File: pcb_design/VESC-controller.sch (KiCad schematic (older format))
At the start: 26 parts, among them J1 GATE_DRIVER_CONN_U, J2 GATE_DRIVER_CONN_V, J3 GATE_DRIVER_CONN_W, J4 micro USB, J5 ACCEL, J6 REGEN, J7 12V, J8 V_BUS, P1 HALL/Encoder, P101 CANBUS, P2 Resolver, P3 PWR_COMM

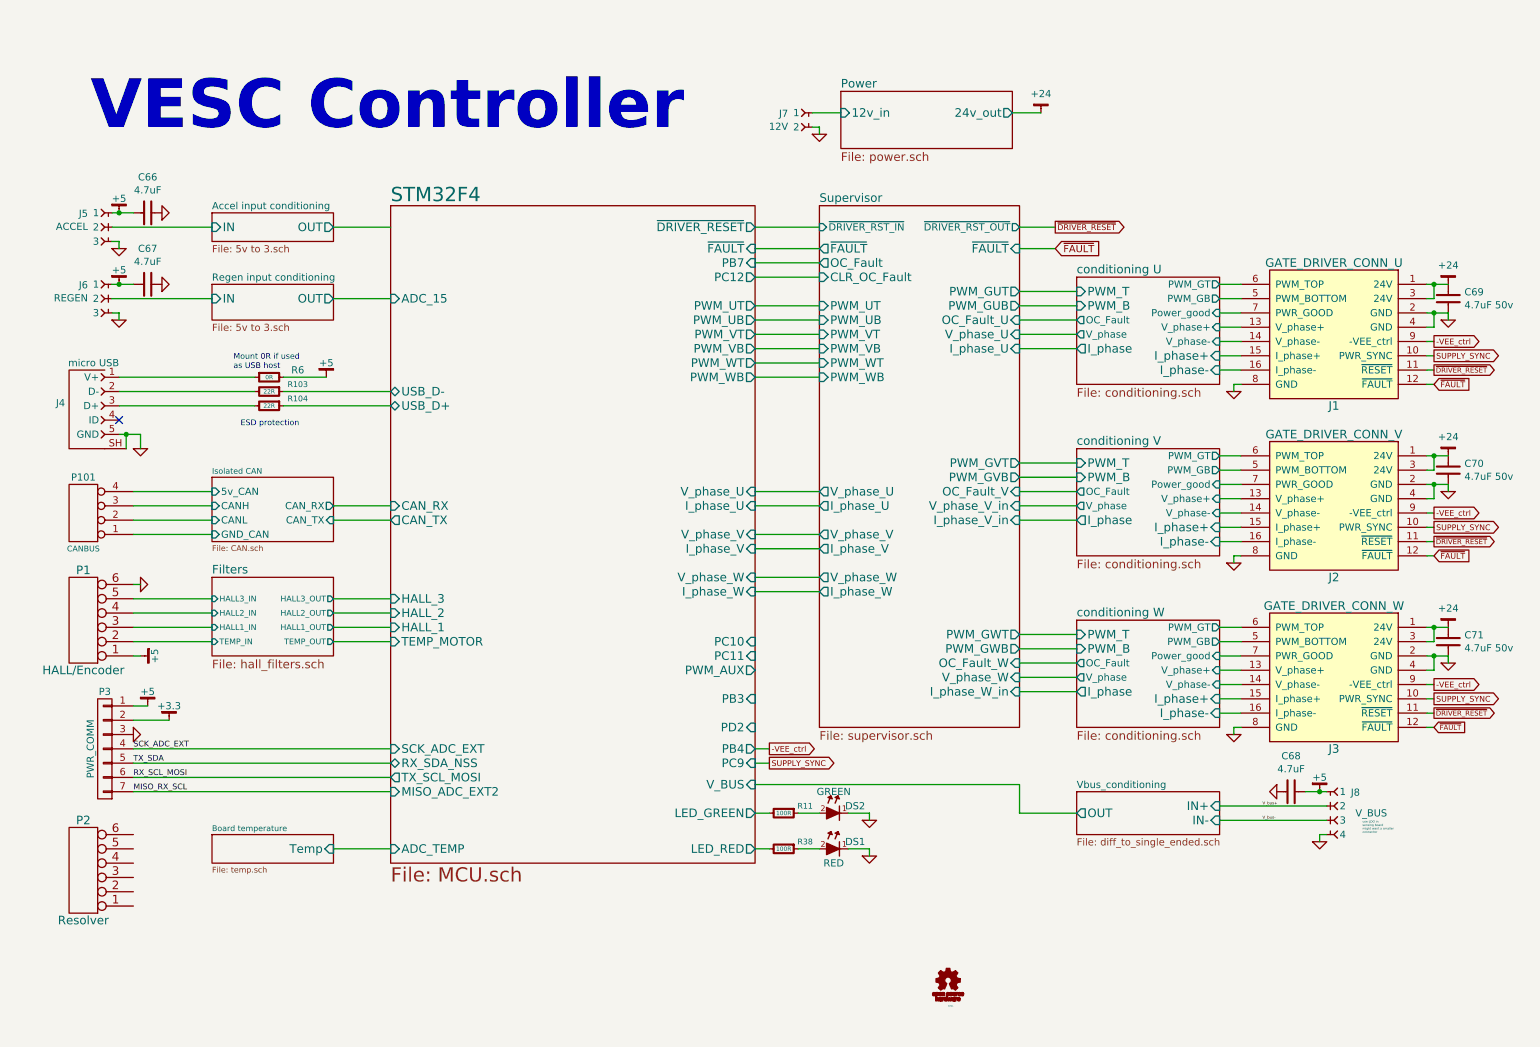
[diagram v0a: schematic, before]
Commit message: More layout. Changed LED pin. Added placeholder for a resolver IC
Signed-off-by: Marcos Chaparro <mchaparro@paltatech.com>
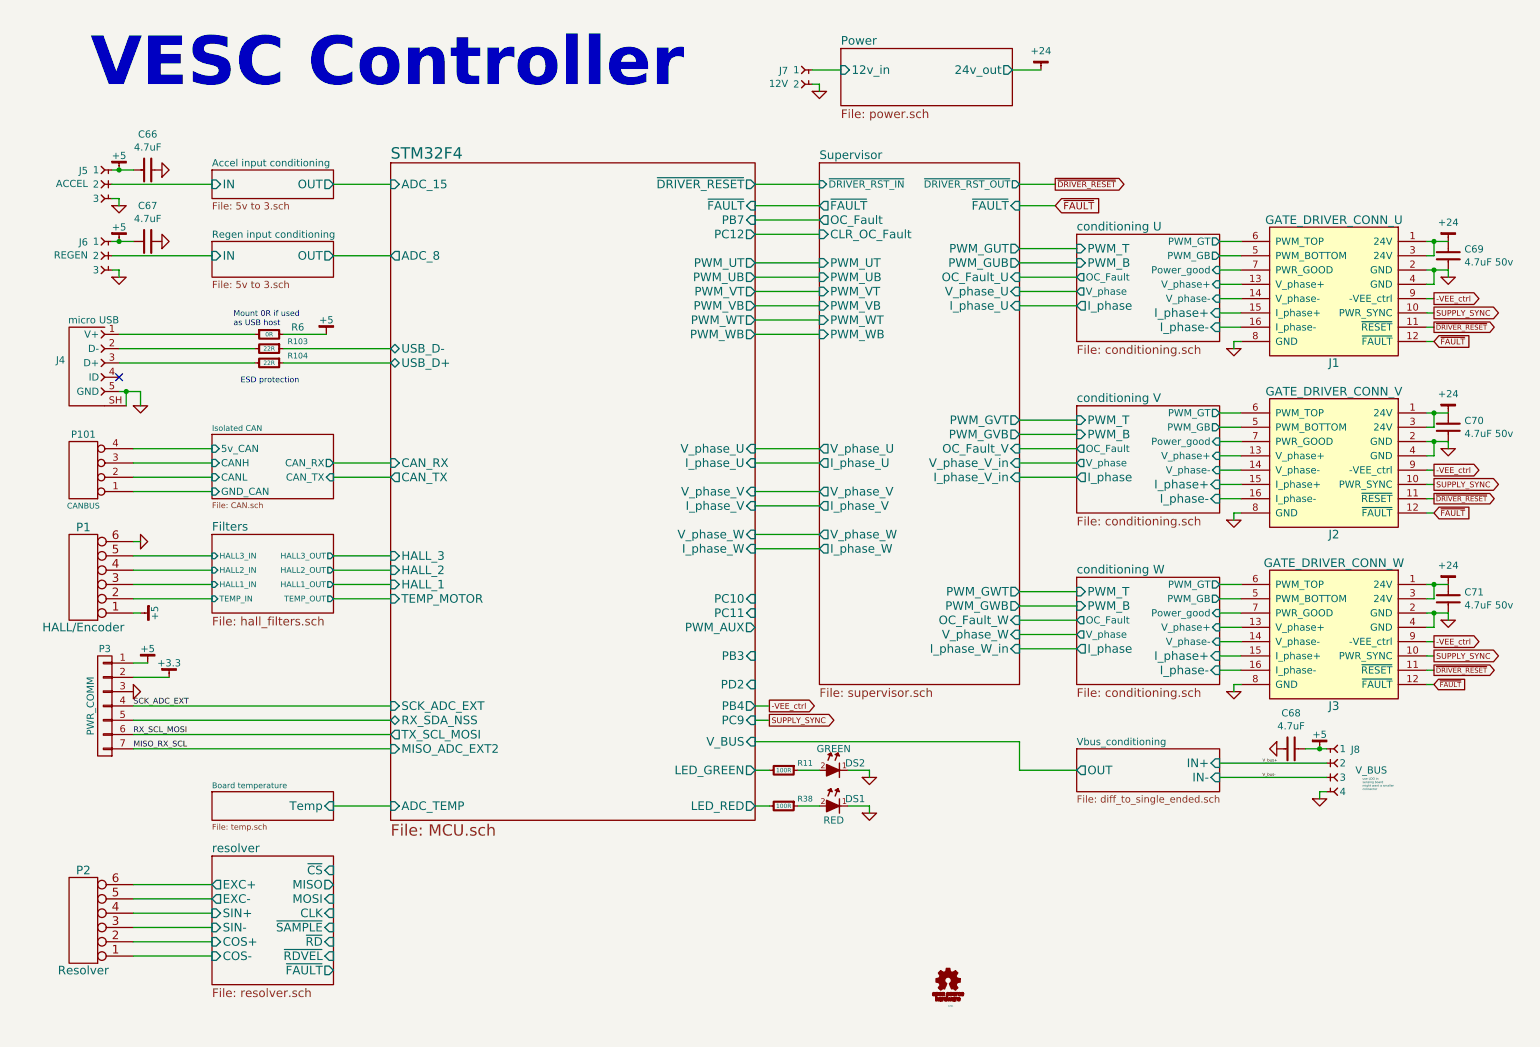
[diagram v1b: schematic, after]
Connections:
- net resolver/COS-: now reaches P2.1
- net resolver/COS+: now reaches P2.2
- net resolver/SIN-: now reaches P2.3
- net resolver/SIN+: now reaches P2.4
- net resolver/EXC-: now reaches P2.5
- net resolver/EXC+: now reaches P2.6
- net TX_SDA renamed STM32F4/RX_SDA_NSS
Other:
- moved on the sheet: C66, C67, C68, C69, C70, C71, DS1, DS2, J1, J2, J3, J4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

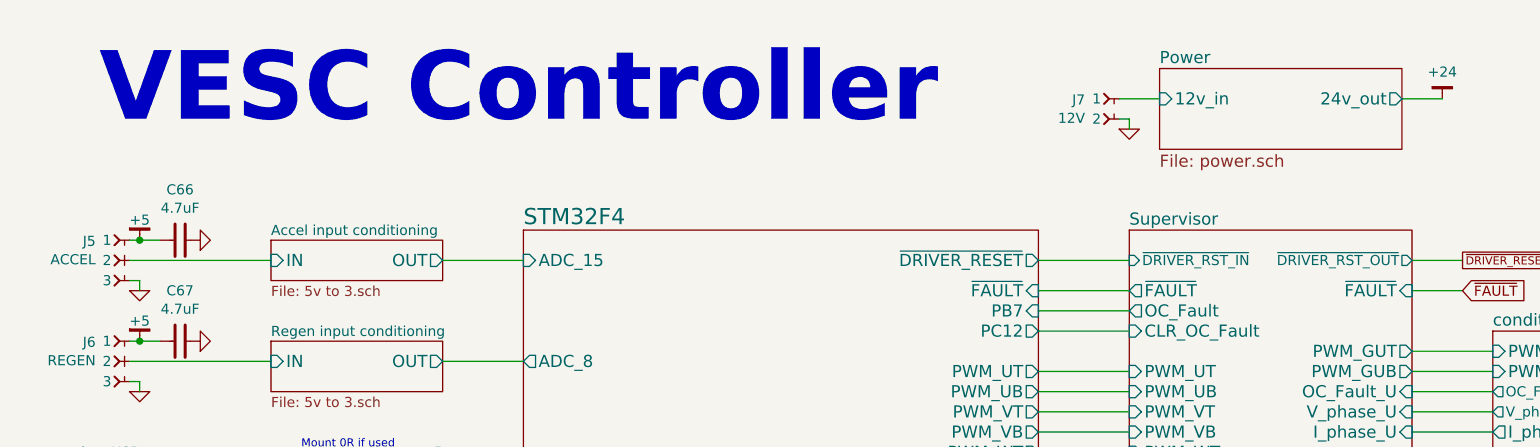
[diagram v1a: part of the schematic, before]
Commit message: Added reverse polarity protection on the isolated side of CON connector. Also, more layout
Signed-off-by: Marcos Chaparro <mchaparro@paltatech.com>
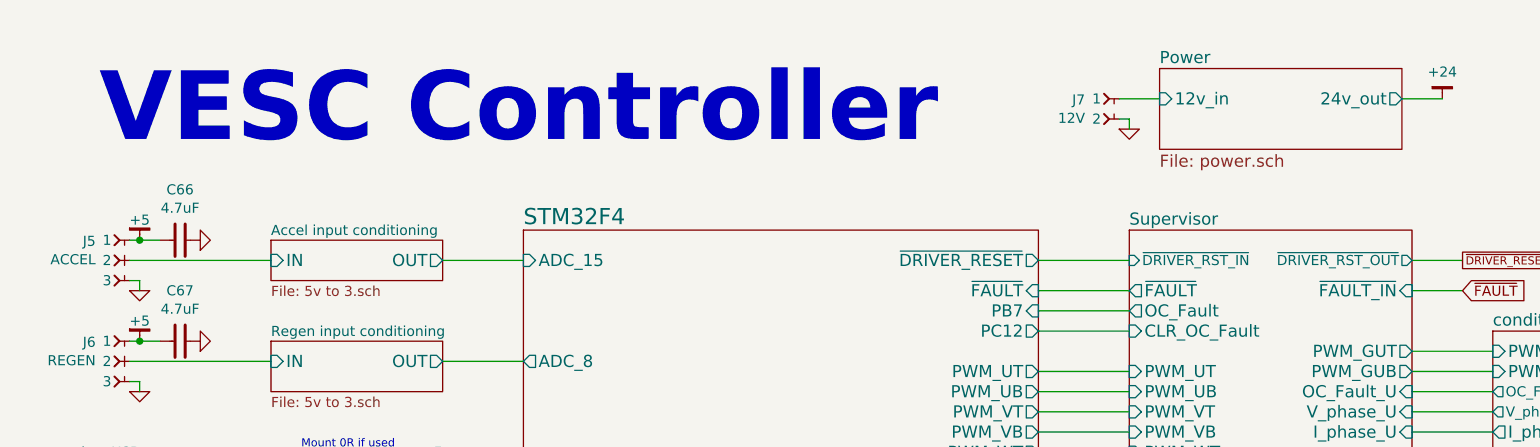
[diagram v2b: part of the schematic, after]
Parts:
- SYM1: footprint mech:OSHW-10mm -> (none)
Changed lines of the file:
@@
 $EndComp
 $Comp
-L GND-RESCUE-BLDC_4 #PWR01
+L GND-RESCUE-BLDC_4 #PWR7
 U 1 1 522DA053
 P 1500 4100
-F 0 "#PWR01" H 1500 4100 30  0001 C CNN
+F 0 "#PWR7" H 1500 4100 30  0001 C CNN
 F 1 "GND" H 1500 4030 30  0001 C CNN
 F 2 "" H 1500 4100 60  0001 C CNN
@@
 $EndComp
 $Comp
-L GND-RESCUE-BLDC_4 #PWR02
+L GND-RESCUE-BLDC_4 #PWR5
 U 1 1 522DA0E2
 P 1450 5150
-F 0 "#PWR02" H 1450 5150 30  0001 C CNN
+F 0 "#PWR5" H 1450 5150 30  0001 C CNN
 F 1 "GND" H 1450 5080 30  0001 C CNN
 F 2 "" H 1450 5150 60  0001 C CNN
@@
 $EndComp
 $Comp
-L GND-RESCUE-BLDC_4 #PWR03
+L GND-RESCUE-BLDC_4 #PWR6
 U 1 1 522DA0FC
 P 1500 3150
-F 0 "#PWR03" H 1500 3150 30  0001 C CNN
+F 0 "#PWR6" H 1500 3150 30  0001 C CNN
 F 1 "GND" H 1500 3080 30  0001 C CNN
 F 2 "" H 1500 3150 60  0001 C CNN
@@
 $EndComp
 $Comp
-L GND-RESCUE-BLDC_4 #PWR04
+L GND-RESCUE-BLDC_4 #PWR16
 U 1 1 53FC131A
 P 6600 6000
-F 0 "#PWR04" H 6600 6000 30  0001 C CNN
+F 0 "#PWR16" H 6600 6000 30  0001 C CNN
 F 1 "GND" H 6600 5930 30  0001 C CNN
 F 2 "" H 6600 6000 60  0001 C CNN
@@
 MISO_RX_SCL
 $Comp
-L GND #PWR05
+L GND #PWR25
 U 1 1 58876637
 P 10650 2250
-F 0 "#PWR05" H 10650 2250 30  0001 C CNN
+F 0 "#PWR25" H 10650 2250 30  0001 C CNN
 F 1 "GND" H 10650 2180 30  0001 C CNN
 F 2 "" H 10650 2250 60  0000 C CNN
@@
 F13 "I_phase-" I R 9050 2600 60
 $EndSheet
-Text Notes 1150 950  0    340  ~ 68
+Text Notes 1150 1050 0    340  ~ 68
 VESC Controller
 Wire Wire Line
@@
 F16 "OC_Fault_W" I R 7650 4650 60
 F17 "OC_Fault" O L 6250 1850 60
-F18 "~FAULT" I R 7650 1750 60
-F19 "~FAULT" O L 6250 1750 60
-F20 "V_phase_U" I R 7650 2350 60
-F21 "V_phase_U" O L 6250 3450 60
-F22 "V_phase_V" O L 6250 3750 60
-F23 "V_phase_W" O L 6250 4050 60
-F24 "V_phase_W" I R 7650 4750 60
-F25 "I_phase_U" I R 7650 2450 60
-F26 "I_phase_U" O L 6250 3550 60
-F27 "I_phase_V_in" I R 7650 3650 60
-F28 "I_phase_W_in" I R 7650 4850 60
-F29 "I_phase_V" O L 6250 3850 60
-F30 "I_phase_W" O L 6250 4150 60
-F31 "V_phase_V_in" I R 7650 3550 60
-F32 "CLR_OC_Fault" I L 6250 1950 60
-F33 "~DRIVER_RST_OUT" O R 7650 1600 50
-F34 "~DRIVER_RST_IN" I L 6250 1600 50
+F18 "~FAULT" O L 6250 1750 60
+F19 "V_phase_U" I R 7650 2350 60
+F20 "V_phase_U" O L 6250 3450 60
+F21 "V_phase_V" O L 6250 3750 60
+F22 "V_phase_W" O L 6250 4050 60
+F23 "V_phase_W" I R 7650 4750 60
+F24 "I_phase_U" I R 7650 2450 60
+F25 "I_phase_U" O L 6250 3550 60
+F26 "I_phase_V_in" I R 7650 3650 60
+F27 "I_phase_W_in" I R 7650 4850 60
+F28 "I_phase_V" O L 6250 3850 60
+F29 "I_phase_W" O L 6250 4150 60
+F30 "V_phase_V_in" I R 7650 3550 60
+F31 "CLR_OC_Fault" I L 6250 1950 60
+F32 "~DRIVER_RST_OUT" O R 7650 1600 50
+F33 "~DRIVER_RST_IN" I L 6250 1600 50
+F34 "~FAULT_IN" I R 7650 1750 60
 $EndSheet
 Wire Wire Line
@@
 	9200 2400 9050 2400
 $Comp
-L GND #PWR06
+L GND #PWR18
 U 1 1 588B9E09
 P 9150 2750
-F 0 "#PWR06" H 9150 2750 30  0001 C CNN
+F 0 "#PWR18" H 9150 2750 30  0001 C CNN
 F 1 "GND" H 9150 2680 30  0001 C CNN
 F 2 "" H 9150 2750 60  0000 C CNN
@@
 	9200 2600 9050 2600
 $Comp
-L GND #PWR07
+L GND #PWR27
 U 1 1 588C277E
 P 10650 3450
-F 0 "#PWR07" H 10650 3450 30  0001 C CNN
+F 0 "#PWR27" H 10650 3450 30  0001 C CNN
 F 1 "GND" H 10650 3380 30  0001 C CNN
 F 2 "" H 10650 3450 60  0000 C CNN
@@
 	9200 3600 9050 3600
 $Comp
-L GND #PWR08
+L GND #PWR19
 U 1 1 588C27A8
 P 9150 3950
-F 0 "#PWR08" H 9150 3950 30  0001 C CNN
+F 0 "#PWR19" H 9150 3950 30  0001 C CNN
 F 1 "GND" H 9150 3880 30  0001 C CNN
 F 2 "" H 9150 3950 60  0000 C CNN
@@
 	8050 4850 7650 4850
 $Comp
-L GND #PWR09
+L GND #PWR29
 U 1 1 588C4E72
 P 10650 4650
-F 0 "#PWR09" H 10650 4650 30  0001 C CNN
+F 0 "#PWR29" H 10650 4650 30  0001 C CNN
 F 1 "GND" H 10650 4580 30  0001 C CNN
 F 2 "" H 10650 4650 60  0000 C CNN
@@
 	9200 4800 9050 4800
 $Comp
-L GND #PWR010
+L GND #PWR20
 U 1 1 588C4E9E
 P 9150 5150
-F 0 "#PWR010" H 9150 5150 30  0001 C CNN
+F 0 "#PWR20" H 9150 5150 30  0001 C CNN
 F 1 "GND" H 9150 5080 30  0001 C CNN
 F 2 "" H 9150 5150 60  0000 C CNN
@@
 	6600 5950 6450 5950
 $Comp
-L GND-RESCUE-BLDC_4 #PWR011
+L GND-RESCUE-BLDC_4 #PWR15
 U 1 1 588CB158
 P 6600 5750
-F 0 "#PWR011" H 6600 5750 30  0001 C CNN
+F 0 "#PWR15" H 6600 5750 30  0001 C CNN
 F 1 "GND" H 6600 5680 30  0001 C CNN
 F 2 "" H 6600 5750 60  0001 C CNN
@@
 $EndComp
 $Comp
-L GND #PWR012
+L GND #PWR2
 U 1 1 588A7EFE
 P 1350 1750
-F 0 "#PWR012" H 1350 1750 30  0001 C CNN
+F 0 "#PWR2" H 1350 1750 30  0001 C CNN
 F 1 "GND" H 1350 1680 30  0001 C CNN
 F 2 "" H 1350 1750 60  0000 C CNN
@@
 	1350 2200 1350 2250
 $Comp
-L GND #PWR013
+L GND #PWR4
 U 1 1 588A9C10
 P 1350 2250
-F 0 "#PWR013" H 1350 2250 30  0001 C CNN
+F 0 "#PWR4" H 1350 2250 30  0001 C CNN
 F 1 "GND" H 1350 2180 30  0001 C CNN
 F 2 "" H 1350 2250 60  0000 C CNN
@@
 	6400 800  6200 800
 $Comp
-L GND #PWR014
+L GND #PWR14
 U 1 1 588CC018
 P 6250 950
-F 0 "#PWR014" H 6250 950 30  0001 C CNN
+F 0 "#PWR14" H 6250 950 30  0001 C CNN
 F 1 "GND" H 6250 880 30  0001 C CNN
 F 2 "" H 6250 950 60  0000 C CNN
@@
 	6250 900  6200 900
 $Comp
-L +5 #PWR015
+L +5 #PWR1
 U 1 1 588B45C6
 P 1350 1500
-F 0 "#PWR015" H 250 -150 30  0001 C CNN
+F 0 "#PWR1" H 250 -150 30  0001 C CNN
 F 1 "+5" H 1350 1600 50  0000 C CNN
 F 2 "" H 250 -200 60  0000 C CNN
@@
 	1300 1500 1450 1500
 $Comp
-L +5 #PWR016
+L +5 #PWR3
 U 1 1 588B5F6B
 P 1350 2000
-F 0 "#PWR016" H 250 350 30  0001 C CNN
+F 0 "#PWR3" H 250 350 30  0001 C CNN
 F 1 "+5" H 1350 2100 50  0000 C CNN
 F 2 "" H 250 300 60  0000 C CNN
@@
 	1300 2000 1450 2000
 $Comp
-L +5 #PWR017
+L +5 #PWR13
 U 1 1 588BB3A4
 P 2800 2650
-F 0 "#PWR017" H 1700 1000 30  0001 C CNN
+F 0 "#PWR13" H 1700 1000 30  0001 C CNN
 F 1 "+5" H 2800 2750 50  0000 C CNN
 F 2 "" H 1700 950 60  0000 C CNN
@@
 $EndComp
 $Comp
-L +5 #PWR018
+L +5 #PWR9
 U 1 1 588BE146
 P 1550 4950
-F 0 "#PWR018" H -50 -250 30  0001 C CNN
+F 0 "#PWR9" H -50 -250 30  0001 C CNN
 F 1 "+5" H 1550 5050 50  0000 C CNN
 F 2 "" H -50 -300 60  0000 C CNN
@@
 $EndComp
 $Comp
-L +3.3 #PWR019
+L +3.3 #PWR12
 U 1 1 588BE494
 P 1700 5050
-F 0 "#PWR019" H 50  -200 30  0001 C CNN
+F 0 "#PWR12" H 50  -200 30  0001 C CNN
 F 1 "+3.3" H 1700 5150 50  0000 C CNN
 F 2 "" H 50  -250 60  0000 C CNN
@@
 $EndComp
 $Comp
-L +5 #PWR020
+L +5 #PWR8
 U 1 1 588C053A
 P 1500 4600
-F 0 "#PWR020" H -100 -600 30  0001 C CNN
+F 0 "#PWR8" H -100 -600 30  0001 C CNN
 F 1 "+5" H 1500 4700 50  0000 C CNN
 F 2 "" H -100 -650 60  0000 C CNN
@@
 	1500 4600 1450 4600
 $Comp
-L +24 #PWR021
+L +24 #PWR17
 U 1 1 588CE8C9
 P 7800 800
-F 0 "#PWR021" H -650 -50 30  0001 C CNN
+F 0 "#PWR17" H -650 -50 30  0001 C CNN
 F 1 "+24" H 7800 933 50  0000 C CNN
 F 2 "" H -650 -100 60  0000 C CNN
@@
 $EndComp
 $Comp
-L +24 #PWR022
+L +24 #PWR24
 U 1 1 588D0DE1
 P 10650 2000
-F 0 "#PWR022" H 10700 2050 30  0001 C CNN
+F 0 "#PWR24" H 10700 2050 30  0001 C CNN
 F 1 "+24" H 10650 2133 50  0000 C CNN
 F 2 "" H -50 -300 60  0000 C CNN
@@
 $EndComp
 $Comp
-L +24 #PWR023
+L +24 #PWR26
 U 1 1 588D1EB4
 P 10650 3200
-F 0 "#PWR023" H 10700 3250 30  0001 C CNN
+F 0 "#PWR26" H 10700 3250 30  0001 C CNN
 F 1 "+24" H 10650 3333 50  0000 C CNN
 F 2 "" H -50 -250 60  0000 C CNN
@@
 $EndComp
 $Comp
-L +24 #PWR024
+L +24 #PWR28
 U 1 1 588D2D5A
 P 10650 4400
-F 0 "#PWR024" H 10700 4450 30  0001 C CNN
+F 0 "#PWR28" H 10700 4450 30  0001 C CNN
 F 1 "+24" H 10650 4533 50  0000 C CNN
 F 2 "" H -50 -300 60  0000 C CNN
@@
 	9800 5750 9050 5750
 $Comp
-L GND #PWR025
+L GND #PWR23
 U 1 1 588E5603
 P 9750 5900
-F 0 "#PWR025" H 9800 5950 30  0001 C CNN
+F 0 "#PWR23" H 9800 5950 30  0001 C CNN
 F 1 "GND" H 0   -270 30  0001 C CNN
 F 2 "" H 0   -200 60  0000 C CNN
@@
 	9750 5850 9800 5850
 $Comp
-L +5 #PWR026
+L +5 #PWR22
 U 1 1 588E703F
 P 9750 5550
-F 0 "#PWR026" H 8650 3900 30  0001 C CNN
+F 0 "#PWR22" H 8650 3900 30  0001 C CNN
 F 1 "+5" H 9750 5650 50  0000 C CNN
 F 2 "" H 8650 3850 60  0000 C CNN
@@
 F 0 "SYM1" H 7150 7050 10  0000 L CNN
 F 1 "OSHW-SCHEM-PCB10mm" H 1000 100 50  0001 C CNN
-F 2 "mech:OSHW-10mm" H 1050 50  50  0001 C CNN
+F 2 "" H 1050 50  50  0001 C CNN
 F 3 "" H 1000 150 50  0000 C CNN
 	1    7150 7200
@@
 $EndComp
 $Comp
-L GND #PWR027
+L GND #PWR21
 U 1 1 588D02C2
 P 9450 5550
-F 0 "#PWR027" H 9500 5600 30  0001 C CNN
+F 0 "#PWR21" H 9500 5600 30  0001 C CNN
 F 1 "GND" H -300 -620 30  0001 C CNN
 F 2 "" H -300 -550 60  0000 C CNN
@@
 $EndComp
 $Comp
-L GND #PWR028
+L GND #PWR10
 U 1 1 588DFDA4
 P 1650 1500
-F 0 "#PWR028" H 1650 1500 30  0001 C CNN
+F 0 "#PWR10" H 1650 1500 30  0001 C CNN
 F 1 "GND" H 1650 1430 30  0001 C CNN
 F 2 "" H 1650 1500 60  0000 C CNN
@@
 Connection ~ 1350 2000
 $Comp
-L GND #PWR029
+L GND #PWR11
 U 1 1 588E1A2D
 P 1650 2000
-F 0 "#PWR029" H 1650 2000 30  0001 C CNN
+F 0 "#PWR11" H 1650 2000 30  0001 C CNN
 F 1 "GND" H 1650 1930 30  0001 C CNN
 F 2 "" H 1650 2000 60  0000 C CNN
